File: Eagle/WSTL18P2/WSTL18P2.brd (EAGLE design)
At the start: 23.5 x 23.5 mm, 24 parts, among them CON1 1X6CONN-1.27-ROUND, CON2 1X6CONN-1.27-ROUND, CON3 1X6CONN-1.27-ROUND, CON4 1X6CONN-1.27-ROUND, T1 ABS07AIG

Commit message: Final corrections for WSTL18P2
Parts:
- moved C6 1.94 mm to (6.35, 13.8)
- moved C7 1.90 mm to (6.35, 8.89), turned to 0 degrees
- moved T1 0.51 mm to (6.35, 11.3)
- moved C1 0.25 mm to (9.14, 13.5)
- moved CON3 0.18 mm to (22.9, 18.4)
- moved CON2 0.18 mm to (3.56, 8.05)
- moved CON1 0.18 mm to (22.9, 8.05)
- moved CON4 0.18 mm to (8.05, 22.9)
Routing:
- net N$1: track 6.22 -> 6.80 mm
- net GND: track 14.7 -> 15.0 mm, vias 24 -> 21
- net RXD0: track 8.45 -> 8.25 mm, vias 1 -> 0
- net PD2: track 11.8 -> 11.7 mm, vias 2 -> 1
- net TXD0: vias 1 -> 0

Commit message: Approved and cleared design rules checks
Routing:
- net PD2: track 11.7 -> 14.6 mm, vias 1 -> 2
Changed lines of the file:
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@@
 <wire x1="14.8336" y1="19.0754" x2="14.4526" y2="19.0754" width="0.254" layer="51"/>
 <wire x1="14.224" y1="19.4564" x2="13.9446" y2="19.4564" width="0.2032" layer="51"/>
-<wire x1="14.1478" y1="18.5166" x2="13.97" y2="18.3388" width="0.254" layer="51"/>
+<wire x1="14.1478" y1="18.3896" x2="13.97" y2="18.2118" width="0.254" layer="51"/>
 <wire x1="10.7442" y1="19.9644" x2="10.4648" y2="19.9644" width="0.254" layer="51"/>
 <wire x1="13.9954" y1="19.0754" x2="14.224" y2="18.8468" width="0.254" layer="51"/>
@@
 <wire x1="8.1534" y1="22.86" x2="8.0518" y2="22.86" width="0.1524" layer="16"/>
 <contactref element="MCU" pad="27"/>
-<wire x1="13.958" y1="15.708" x2="13.958" y2="18.022" width="0.1524" layer="1"/>
-<wire x1="13.958" y1="18.022" x2="14.7066" y2="18.5674" width="0.1524" layer="1"/>
-<wire x1="14.7066" y1="18.5674" x2="14.6558" y2="18.6436" width="0.1524" layer="1"/>
+<wire x1="13.958" y1="15.708" x2="13.958" y2="17.768" width="0.1524" layer="1"/>
 <wire x1="10.6172" y1="20.3962" x2="12.0142" y2="20.3962" width="0.1524" layer="1"/>
 <wire x1="12.0142" y1="20.3962" x2="12.233" y2="20.615" width="0.1524" layer="1"/>
@@
 <wire x1="13.9446" y1="19.431" x2="11.5824" y2="19.431" width="0.1524" layer="16"/>
 <wire x1="11.5824" y1="19.431" x2="10.6172" y2="20.3962" width="0.1524" layer="16"/>
+<wire x1="13.958" y1="17.768" x2="14.6558" y2="18.4658" width="0.1524" layer="1"/>
+<wire x1="14.6558" y1="18.4658" x2="14.6558" y2="18.6436" width="0.1524" layer="1"/>
 </signal>
 <signal name="SCL0" class="2">
@@
 <contactref element="CON2" pad="1"/>
 <via x="21.5138" y="14.5542" extent="1-16" drill="0.3048"/>
-<via x="18.4404" y="18.288" extent="1-16" drill="0.3048"/>
+<via x="18.3642" y="18.1102" extent="1-16" drill="0.3048"/>
 <via x="16.8656" y="3.8862" extent="1-16" drill="0.3048"/>
 <via x="14.0462" y="5.2832" extent="1-16" drill="0.3048"/>
@@
 <via x="9.271" y="23.368" extent="1-16" drill="0.3048"/>
 <contactref element="UART" pad="4"/>
-<wire x1="16.7386" y1="11.0454" x2="16.637" y2="10.922" width="0.2032" layer="1"/>
 <wire x1="10.382921875" y1="23.805475" x2="9.652" y2="23.0886" width="0.2032" layer="1"/>
 <wire x1="9.652" y1="23.0886" x2="9.525" y2="22.987" width="0.2032" layer="1"/>
@@
 <wire x1="18.3896" y1="8.2042" x2="16.8656" y2="8.2042" width="0.1524" layer="1"/>
 <wire x1="16.8656" y1="8.2042" x2="14.958" y2="10.1118" width="0.1524" layer="1"/>
-<wire x1="17.5768" y1="7.1374" x2="18.975478125" y2="5.357721875" width="0.1524" layer="16"/>
-<wire x1="18.975478125" y1="5.357721875" x2="20.165921875" y2="5.357721875" width="0.1524" layer="16"/>
 <wire x1="14.958" y1="10.708" x2="14.958" y2="10.1118" width="0.1524" layer="1"/>
 <wire x1="16.1876125" y1="6.23323125" x2="17.09178125" y2="7.1374" width="0.1524" layer="1"/>
 <wire x1="17.09178125" y1="7.1374" x2="17.5768" y2="7.1374" width="0.1524" layer="1"/>
+<wire x1="17.5768" y1="7.1374" x2="18.415" y2="6.2992" width="0.1524" layer="16"/>
+<wire x1="18.415" y1="6.2992" x2="18.415" y2="5.969" width="0.1524" layer="16"/>
+<wire x1="18.415" y1="5.969" x2="18.796" y2="5.588" width="0.1524" layer="16"/>
+<wire x1="18.796" y1="5.588" x2="19.93564375" y2="5.588" width="0.1524" layer="16"/>
+<wire x1="19.93564375" y1="5.588" x2="20.165921875" y2="5.357721875" width="0.1524" layer="16"/>
 </signal>
 <signal name="SCK0" class="2">
@@
 <wire x1="16.51" y1="20.6756" x2="17.1704" y2="21.336" width="0.1524" layer="1"/>
 <via x="17.1704" y="21.336" extent="1-16" drill="0.3048" shape="octagon"/>
-<wire x1="17.1704" y1="21.0566" x2="18.542" y2="19.685" width="0.1524" layer="16"/>
-<wire x1="17.1704" y1="21.0566" x2="17.1704" y2="21.336" width="0.1524" layer="16"/>
-<wire x1="18.542" y1="19.685" x2="18.542" y2="19.685" width="0" layer="19" extent="1-16"/>
+<via x="19.304" y="18.923" extent="1-16" drill="0.3048" shape="octagon"/>
+<wire x1="19.304" y1="18.923" x2="18.542" y2="19.685" width="0.1524" layer="1"/>
+<wire x1="17.1704" y1="21.336" x2="17.1704" y2="21.3106" width="0.1524" layer="16"/>
+<wire x1="17.1704" y1="21.3106" x2="17.78" y2="20.701" width="0.1524" layer="16"/>
+<wire x1="17.78" y1="20.701" x2="17.78" y2="19.304" width="0.1524" layer="16"/>
+<wire x1="17.78" y1="19.304" x2="18.161" y2="18.923" width="0.1524" layer="16"/>
+<wire x1="18.161" y1="18.923" x2="19.304" y2="18.923" width="0.1524" layer="16"/>
 </signal>
 <signal name="PE2">

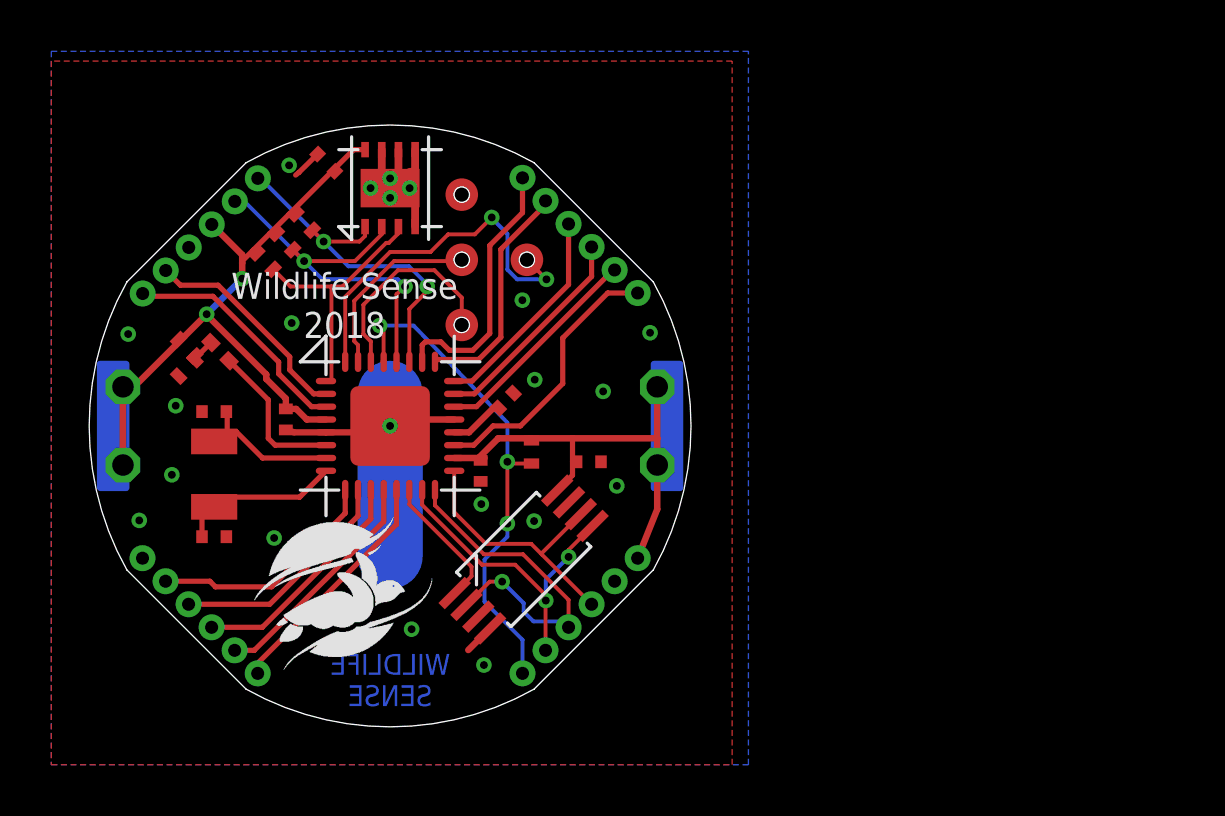
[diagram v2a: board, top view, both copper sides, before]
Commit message: Center-alligned all 4 6-wire headers
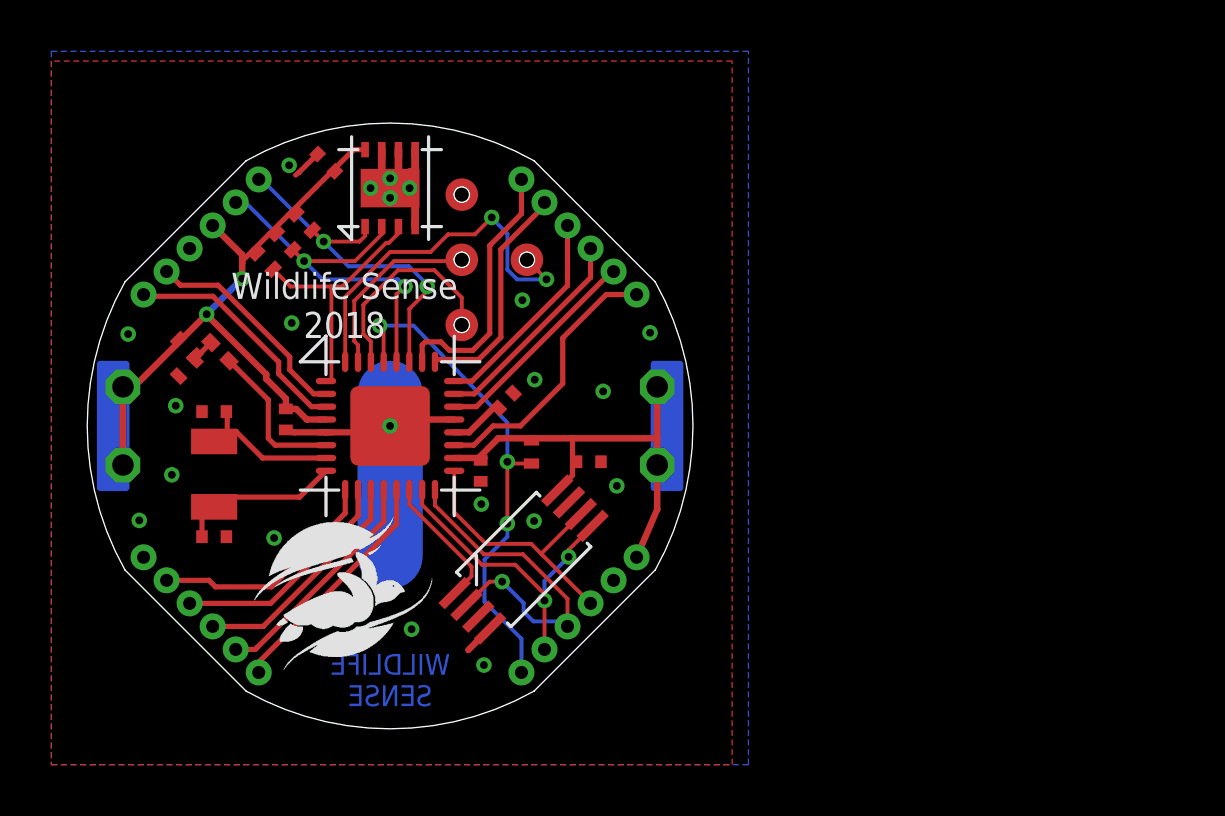
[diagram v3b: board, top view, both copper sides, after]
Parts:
- CON1, CON2, CON3, CON4: value 1X6CONN-1.27-ROUND -> 1X6CONN-1.27-ROUND_CENTERED; device AVR_ISP_127:1X6_1.27_ROUND -> AVR_ISP_127:1X6_1.27_ROUND_CENTERED
- moved CON2 3.18 mm to (5.84, 5.84)
- moved CON1 3.18 mm to (20.6, 5.84)
- moved CON4 3.18 mm to (5.84, 20.6)
- moved CON3 3.16 mm to (20.6, 20.6)
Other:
- board size 23.5 x 23.5 mm -> 23.6 x 23.6 mm
